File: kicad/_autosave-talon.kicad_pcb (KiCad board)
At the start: 2 copper layers, 157.7 x 112.7 mm, 38 parts, among them U1 nice_nano

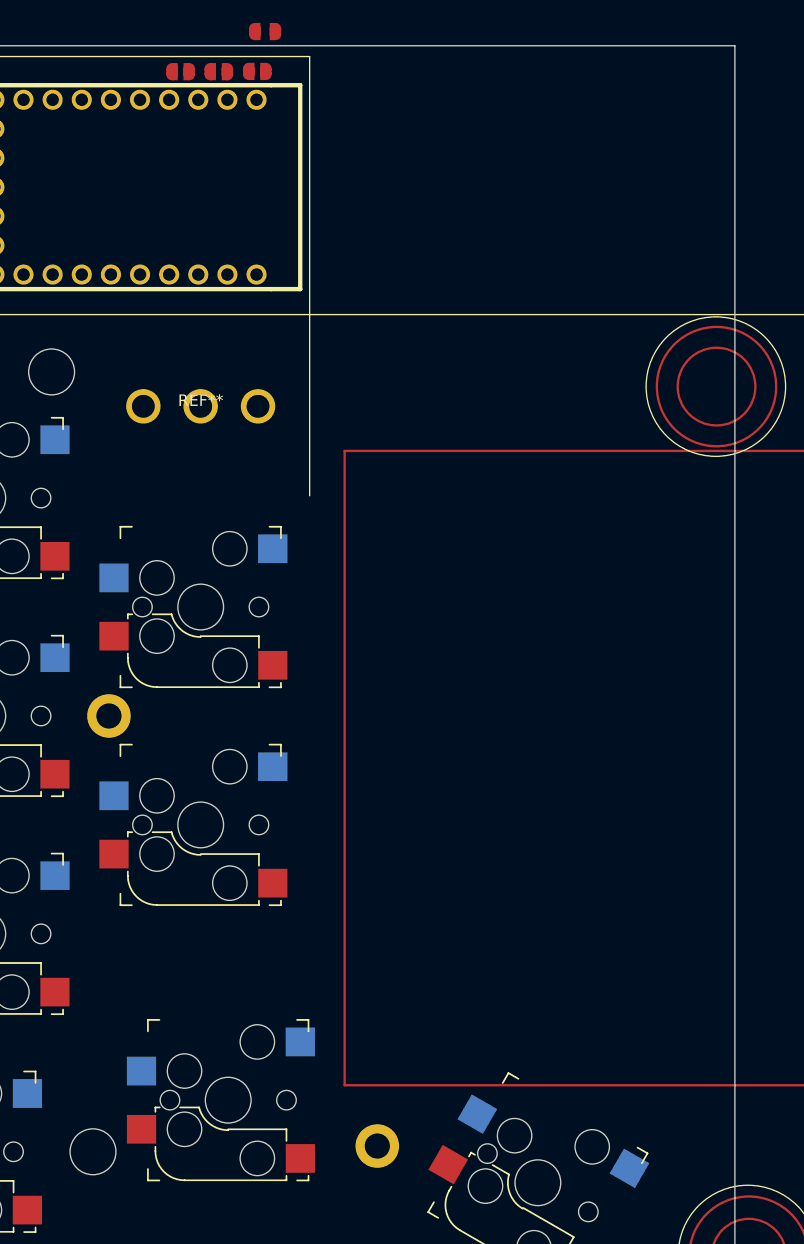
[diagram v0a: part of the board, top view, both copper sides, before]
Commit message: fully constrained key plate
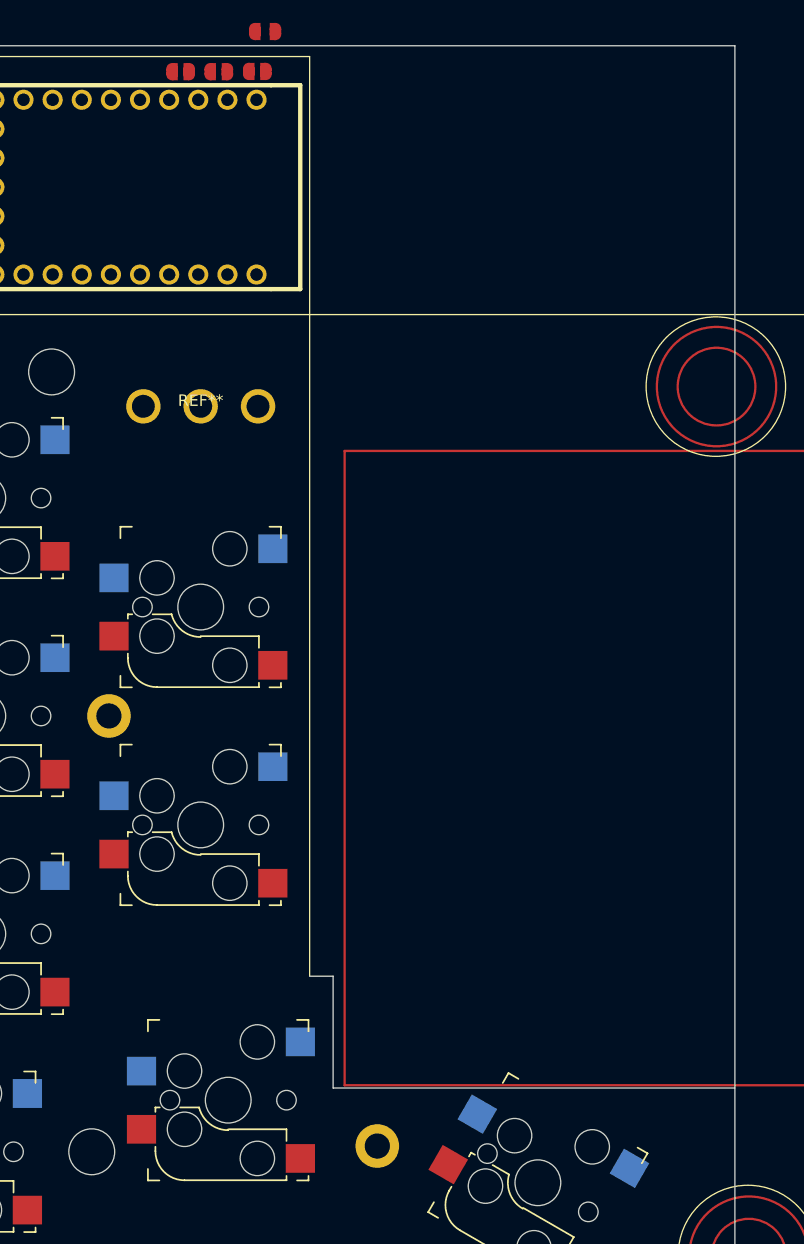
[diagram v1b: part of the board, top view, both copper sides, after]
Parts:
- moved REF** 0.11 mm to (178.5, 142.0)
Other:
- outline, holes or cut-outs redrawn
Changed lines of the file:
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@@
   )
   (footprint "footprints:through_hole_m2" locked (layer "F.Cu")
-    (at 178.61 142)
+    (at 178.5 142)
     (attr smd)
     (fp_text reference "REF**" (at 0 -0.5 unlocked) (layer "F.SilkS") hide
@@
   (gr_line locked (start 159.5 46.5) (end 197.5 46.5)
     (stroke (width 0.1) (type default)) (layer "F.SilkS"))
-  (gr_line locked (start 197.5 46.5) (end 197.5 84.8)
+  (gr_line (start 197.5 46.5) (end 197.5 126.69)
     (stroke (width 0.1) (type default)) (layer "F.SilkS"))
   (gr_circle (center 235.718882 151) (end 241.8 151)
@@
   (gr_circle (center 232.92 75.28) (end 239.001118 75.28)
     (stroke (width 0.1) (type default)) (fill none) (layer "F.SilkS"))
+  (gr_line (start 197.5 126.69) (end 199.55 126.69)
+    (stroke (width 0.1) (type default)) (layer "Edge.Cuts"))
+  (gr_line (start 199.55 126.69) (end 199.55 136.44)
+    (stroke (width 0.1) (type default)) (layer "Edge.Cuts"))
   (gr_rect (start 76.91 45.56) (end 234.58 158.24)
     (stroke (width 0.1) (type default)) (fill none) (layer "Edge.Cuts"))
+  (gr_line (start 199.55 136.44) (end 234.57 136.44)
+    (stroke (width 0.1) (type default)) (layer "Edge.Cuts"))
 )
